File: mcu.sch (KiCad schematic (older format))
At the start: 44 parts

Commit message: Add harmonic filter to ESP32 RF front end.
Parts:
- added C? (x2): CAP-EIA0402, footprints_generic:CAPC100X50X55L30N, symbol gz_Ceramic-Capacitors:CAP-EIA0402
- added L?: IND-EIA0201, footprints_generic:INDC60X30X42L15L, symbol gz_Fixed-Inductors:IND-EIA0201
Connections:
- wire segments 165 -> 172
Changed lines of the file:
@@
 Wire Wire Line
 	3400 4750 3900 4750
+$Comp
+L gz_Ceramic-Capacitors:CAP-EIA0402 C?
+U 1 1 604B4874
+P 6250 5800
+F 0 "C?" V 6200 5950 50  0000 L CNN
+F 1 "CAP-EIA0402" H 6650 6900 50  0001 L CNN
+F 2 "footprints_generic:CAPC100X50X55L30N" H 2950 10150 50  0001 L CNN
+F 3 "${KEMET_MLCC_BASE}C0402C150J5GACTU" H 2950 10250 50  0001 L CNN
+F 4 "Digikey" H 6650 6800 50  0001 L CNN "Vendor"
+F 5 "399-1014-1-ND" H 7000 6800 50  0001 L CNN "Vendor_PN"
+F 6 "KEMET" H 6650 6700 50  0001 L CNN "Manufacturer"
+F 7 "C0402C150J5GACTU" H 7250 6700 50  0001 L CNN "MPN"
+F 8 "Capacitors" H 2950 10550 50  0001 L CNN "Category"
+F 9 "Ceramic Capacitors" H 2950 10650 50  0001 L CNN "Family"
+F 10 "Yes" V 6200 6100 50  0001 L CNN "Fit"
+F 11 "15pF" V 6300 5950 50  0000 L CNN "Capacitance"
+F 12 "±5%" V 6300 6200 50  0000 L CNN "Tolerance"
+F 13 "50V" V 6400 6200 50  0000 L CNN "Voltage"
+F 14 "C0G" V 6400 5950 50  0000 L CNN "Dielectric"
+F 15 "EIA0402" V 6500 5950 50  0000 L CNN "Package"
+	1    6250 5800
+	0    1    1    0
+$EndComp
+$Comp
+L gz_Ceramic-Capacitors:CAP-EIA0402 C?
+U 1 1 604B72FD
+P 7250 5800
+F 0 "C?" V 7200 5950 50  0000 L CNN
+F 1 "CAP-EIA0402" H 7650 6900 50  0001 L CNN
+F 2 "footprints_generic:CAPC100X50X55L30N" H 3950 10150 50  0001 L CNN
+F 3 "${KEMET_MLCC_BASE}C0402C130J5GACTU" H 3950 10250 50  0001 L CNN
+F 4 "Digikey" H 7650 6800 50  0001 L CNN "Vendor"
+F 5 "399-8946-1-ND" H 8000 6800 50  0001 L CNN "Vendor_PN"
+F 6 "KEMET" H 7650 6700 50  0001 L CNN "Manufacturer"
+F 7 "C0402C130J5GACTU" H 8250 6700 50  0001 L CNN "MPN"
+F 8 "Capacitors" H 3950 10550 50  0001 L CNN "Category"
+F 9 "Ceramic Capacitors" H 3950 10650 50  0001 L CNN "Family"
+F 10 "Yes" V 7200 6100 50  0001 L CNN "Fit"
+F 11 "13pF" V 7300 5950 50  0000 L CNN "Capacitance"
+F 12 "±5%" V 7300 6200 50  0000 L CNN "Tolerance"
+F 13 "50V" V 7400 6200 50  0000 L CNN "Voltage"
+F 14 "C0G" V 7400 5950 50  0000 L CNN "Dielectric"
+F 15 "EIA0402" V 7500 5950 50  0000 L CNN "Package"
+	1    7250 5800
+	0    1    1    0
+$EndComp
+$Comp
+L gz_Fixed-Inductors:IND-EIA0201 L?
+U 1 1 604BFB5E
+P 6750 5600
+F 0 "L?" H 6775 5972 50  0000 C CNN
+F 1 "IND-EIA0201" H 7200 7400 50  0001 L CNN
+F 2 "footprints_generic:INDC60X30X42L15L" H 7200 7300 50  0001 L CNN
+F 3 "${MURATA_BASE}LQP03HQ0N6W02%23" H 3450 10050 50  0001 L CNN
+F 4 "Digikey" H 7200 7200 50  0001 L CNN "Vendor"
+F 5 "490-13844-1-ND" H 7550 7200 50  0001 L CNN "Vendor_PN"
+F 6 "Murata Electronics" H 7200 7100 50  0001 L CNN "Manufacturer"
+F 7 "LQP03HQ0N6W02#" H 8000 7100 50  0001 L CNN "MPN"
+F 8 "Inductors, Coils, Chokes" H 7200 7000 50  0001 L CNN "Category"
+F 9 "Fixed Inductors" H 7200 6900 50  0001 L CNN "Family"
+F 10 "Yes" H 6600 6050 50  0001 L CNN "Fit"
+F 11 "0.6Nh" H 6775 5881 50  0000 C CNN "Inductance"
+F 12 "±0.05Nh" H 6775 5790 50  0000 C CNN "Tolerance"
+F 13 "Q 20 @ 500MHz" H 7200 6800 50  0001 L CNN "Quality Factor"
+F 14 "DCR 40mr" H 7200 6700 50  0001 L CNN "DCR"
+F 15 "SRF 20GHz" H 7200 6600 50  0001 L CNN "SRF"
+F 16 "1.1A" H 7200 6500 50  0001 L CNN "Current"
+F 17 "FILM" H 7200 6400 50  0001 L CNN "Type"
+F 18 "EIA0201" H 6775 5699 50  0000 C CNN "Package"
+	1    6750 5600
+	1    0    0    -1
+$EndComp
+Wire Wire Line
+	5950 5600 6250 5600
+Wire Wire Line
+	6250 5700 6250 5600
+Connection ~ 6250 5600
+Wire Wire Line
+	6250 5600 6650 5600
+Wire Wire Line
+	6900 5600 7250 5600
+Wire Wire Line
+	7250 5600 7250 5700
+Wire Wire Line
+	7250 5900 7250 5950
+Wire Wire Line
+	6250 5900 6250 5950
+$Comp
+L gz_Power-Symbols:GND #PWR?
+U 1 1 604F291C
+P 6250 5950
+F 0 "#PWR?" H 6250 5700 50  0001 C CNN
+F 1 "GND" H 6255 5777 50  0000 C CNN
+F 2 "" H 6250 5950 50  0001 C CNN
+F 3 "" H 6250 5950 50  0001 C CNN
+	1    6250 5950
+	1    0    0    -1
+$EndComp
+$Comp
+L gz_Power-Symbols:GND #PWR?
+U 1 1 604F32B0
+P 7250 5950
+F 0 "#PWR?" H 7250 5700 50  0001 C CNN
+F 1 "GND" H 7255 5777 50  0000 C CNN
+F 2 "" H 7250 5950 50  0001 C CNN
+F 3 "" H 7250 5950 50  0001 C CNN
+	1    7250 5950
+	1    0    0    -1
+$EndComp
 $EndSCHEMATC

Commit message: Add antenna matching section.
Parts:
- removed L?: IND-EIA0201, footprints_generic:INDC60X30X42L15L, symbol gz_Fixed-Inductors:IND-EIA0201
- added L?: IND-EIA0402, footprints_generic:INDC100X50X55L25N, symbol gz_Fixed-Inductors:IND-EIA0402
- added Z? (x3): Z-EIA0402, footprints_generic:RESC100X50X40L25NN, symbol gz_Generic-Impedance-Surface-Mount:Z-EIA0402
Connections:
- wire segments 172 -> 180
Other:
- note added: "2445MHz\nQ = 10"
- note added: "30 +j10"
- note added: "50R"
- note added: "Antenna Matching\n"
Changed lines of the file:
@@
 	0    1    1    0
-$EndComp
-$Comp
-L gz_Fixed-Inductors:IND-EIA0201 L?
-U 1 1 604BFB5E
-P 6750 5600
-F 0 "L?" H 6775 5972 50  0000 C CNN
-F 1 "IND-EIA0201" H 7200 7400 50  0001 L CNN
-F 2 "footprints_generic:INDC60X30X42L15L" H 7200 7300 50  0001 L CNN
-F 3 "${MURATA_BASE}LQP03HQ0N6W02%23" H 3450 10050 50  0001 L CNN
-F 4 "Digikey" H 7200 7200 50  0001 L CNN "Vendor"
-F 5 "490-13844-1-ND" H 7550 7200 50  0001 L CNN "Vendor_PN"
-F 6 "Murata Electronics" H 7200 7100 50  0001 L CNN "Manufacturer"
-F 7 "LQP03HQ0N6W02#" H 8000 7100 50  0001 L CNN "MPN"
-F 8 "Inductors, Coils, Chokes" H 7200 7000 50  0001 L CNN "Category"
-F 9 "Fixed Inductors" H 7200 6900 50  0001 L CNN "Family"
-F 10 "Yes" H 6600 6050 50  0001 L CNN "Fit"
-F 11 "0.6Nh" H 6775 5881 50  0000 C CNN "Inductance"
-F 12 "±0.05Nh" H 6775 5790 50  0000 C CNN "Tolerance"
-F 13 "Q 20 @ 500MHz" H 7200 6800 50  0001 L CNN "Quality Factor"
-F 14 "DCR 40mr" H 7200 6700 50  0001 L CNN "DCR"
-F 15 "SRF 20GHz" H 7200 6600 50  0001 L CNN "SRF"
-F 16 "1.1A" H 7200 6500 50  0001 L CNN "Current"
-F 17 "FILM" H 7200 6400 50  0001 L CNN "Type"
-F 18 "EIA0201" H 6775 5699 50  0000 C CNN "Package"
-	1    6750 5600
-	1    0    0    -1
 $EndComp
 Wire Wire Line
@@
 	1    0    0    -1
 $EndComp
+$Comp
+L gz_Fixed-Inductors:IND-EIA0402 L?
+U 1 1 604DAC9B
+P 6750 5600
+F 0 "L?" H 6650 5900 50  0000 L CNN
+F 1 "IND-EIA0402" H 7200 7400 50  0001 L CNN
+F 2 "footprints_generic:INDC100X50X55L25N" H 7200 7300 50  0001 L CNN
+F 3 "${TDK_BASE}MLG1005S0N6BT000" H 3450 10050 50  0001 L CNN
+F 4 "Digikey" H 7200 7200 50  0001 L CNN "Vendor"
+F 5 "445-16237-1-ND" H 7550 7200 50  0001 L CNN "Vendor_PN"
+F 6 "TDK Corporation" H 7200 7100 50  0001 L CNN "Manufacturer"
+F 7 "MLG1005S0N6BT000" H 8000 7100 50  0001 L CNN "MPN"
+F 8 "Inductors, Coils, Chokes" H 7200 7000 50  0001 L CNN "Category"
+F 9 "Fixed Inductors" H 7200 6900 50  0001 L CNN "Family"
+F 10 "Yes" H 6600 6050 50  0001 L CNN "Fit"
+F 11 "0.6nH" H 6650 5800 50  0000 L CNN "Inductance"
+F 12 "±0.1nH" H 6900 5800 50  0000 L CNN "Tolerance"
+F 13 "Q 10 @ 100MHz" H 7200 6800 50  0001 L CNN "Quality Factor"
+F 14 "DCR 100mR" H 7200 6700 50  0001 L CNN "DCR"
+F 15 "SRF 10GHz" H 7200 6600 50  0001 L CNN "SRF"
+F 16 "Imax 1A" H 7200 6500 50  0001 L CNN "Current"
+F 17 "ML" H 7200 6400 50  0001 L CNN "Type"
+F 18 "EIA0402" H 6650 5700 50  0000 L CNN "Package"
+	1    6750 5600
+	1    0    0    -1
+$EndComp
+Text Notes 5700 5950 0    50   ~ 0
+30 +j10
+Wire Notes Line
+	7850 5150 7850 6250
+Wire Notes Line
+	7850 6250 6050 6250
+Wire Notes Line
+	6050 6250 6050 5150
+Wire Notes Line
+	6050 5150 7850 5150
+Wire Notes Line style solid
+	6000 5850 6000 5650
+Wire Notes Line style solid
+	6000 5650 5900 5650
+Wire Notes Line style solid
+	5900 5650 5925 5625
+Wire Notes Line style solid
+	5900 5650 5925 5675
+Text Notes 7900 5950 0    50   ~ 0
+50R
+Wire Notes Line style solid
+	8000 5850 8000 5650
+Wire Notes Line style solid
+	8000 5650 7900 5650
+Wire Notes Line style solid
+	7900 5650 7925 5625
+Wire Notes Line style solid
+	7900 5650 7925 5675
+Connection ~ 7250 5600
+Text Notes 7450 5350 0    50   ~ 0
+2445MHz\nQ = 10
+Wire Wire Line
+	8650 5650 8650 5600
+Connection ~ 8650 5600
+Wire Wire Line
+	9250 5600 9500 5600
+Wire Wire Line
+	9500 5600 9500 5650
+Wire Wire Line
+	8650 5950 8650 6000
+$Comp
+L gz_Power-Symbols:GND #PWR?
+U 1 1 605A2506
+P 8650 6000
+F 0 "#PWR?" H 8650 5750 50  0001 C CNN
+F 1 "GND" H 8655 5827 50  0000 C CNN
+F 2 "" H 8650 6000 50  0001 C CNN
+F 3 "" H 8650 6000 50  0001 C CNN
+	1    8650 6000
+	1    0    0    -1
+$EndComp
+Wire Notes Line
+	10250 5150 10250 6250
+Wire Notes Line
+	10250 6250 8450 6250
+Wire Notes Line
+	8450 6250 8450 5150
+Wire Notes Line
+	8450 5150 10250 5150
+Text Notes 10300 5950 0    50   ~ 0
+50R
+Wire Notes Line style solid
+	10400 5850 10400 5650
+Wire Notes Line style solid
+	10400 5650 10300 5650
+Wire Notes Line style solid
+	10300 5650 10325 5625
+Wire Notes Line style solid
+	10300 5650 10325 5675
+Wire Wire Line
+	9500 5600 10400 5600
+Connection ~ 9500 5600
+Wire Wire Line
+	7250 5600 8650 5600
+Text Notes 8400 5950 2    50   ~ 0
+50R
+Wire Notes Line style solid
+	8300 5850 8300 5650
+Wire Notes Line style solid
+	8300 5650 8400 5650
+Wire Notes Line style solid
+	8400 5650 8375 5625
+Wire Notes Line style solid
+	8400 5650 8375 5675
+$Comp
+L gz_Generic-Impedance-Surface-Mount:Z-EIA0402 Z?
+U 1 1 605FEF00
+P 8650 5800
+F 0 "Z?" V 8559 5853 50  0000 L CNN
+F 1 "Z-EIA0402" H 9450 6700 50  0001 L CNN
+F 2 "footprints_generic:RESC100X50X40L25NN" H 5350 10150 50  0001 L CNN
+F 3 "" H 5350 10250 50  0001 L CNN
+F 4 "TBD" H 9450 6600 50  0001 L CNN "Vendor"
+F 5 "TBD" H 9800 6600 50  0001 L CNN "Vendor_PN"
+F 6 "TBD" H 9450 6500 50  0001 L CNN "Manufacturer"
+F 7 "TBD" H 10050 6500 50  0001 L CNN "MPN"
+F 8 "TBD" H 5350 10550 50  0001 L CNN "Category"
+F 9 "TBD" H 5350 10650 50  0001 L CNN "Family"
+F 10 "NF" V 8650 5853 50  0000 L CNN "Fit"
+F 11 "TBD" V 8695 5853 50  0001 L CNN "Nominal"
+F 12 "TBD" V 8695 5853 50  0001 L CNN "Tolerance"
+F 13 "EIA0402" V 8741 5853 50  0000 L CNN "Package"
+	1    8650 5800
+	0    1    1    0
+$EndComp
+Wire Wire Line
+	9500 5950 9500 6000
+$Comp
+L gz_Power-Symbols:GND #PWR?
+U 1 1 6063A4C0
+P 9500 6000
+F 0 "#PWR?" H 9500 5750 50  0001 C CNN
+F 1 "GND" H 9505 5827 50  0000 C CNN
+F 2 "" H 9500 6000 50  0001 C CNN
+F 3 "" H 9500 6000 50  0001 C CNN
+	1    9500 6000
+	1    0    0    -1
+$EndComp
+$Comp
+L gz_Generic-Impedance-Surface-Mount:Z-EIA0402 Z?
+U 1 1 6063A4D0
+P 9500 5800
+F 0 "Z?" V 9409 5853 50  0000 L CNN
+F 1 "Z-EIA0402" H 10300 6700 50  0001 L CNN
+F 2 "footprints_generic:RESC100X50X40L25NN" H 6200 10150 50  0001 L CNN
+F 3 "" H 6200 10250 50  0001 L CNN
+F 4 "TBD" H 10300 6600 50  0001 L CNN "Vendor"
+F 5 "TBD" H 10650 6600 50  0001 L CNN "Vendor_PN"
+F 6 "TBD" H 10300 6500 50  0001 L CNN "Manufacturer"
+F 7 "TBD" H 10900 6500 50  0001 L CNN "MPN"
+F 8 "TBD" H 6200 10550 50  0001 L CNN "Category"
+F 9 "TBD" H 6200 10650 50  0001 L CNN "Family"
+F 10 "NF" V 9500 5853 50  0000 L CNN "Fit"
+F 11 "TBD" V 9545 5853 50  0001 L CNN "Nominal"
+F 12 "TBD" V 9545 5853 50  0001 L CNN "Tolerance"
+F 13 "EIA0402" V 9591 5853 50  0000 L CNN "Package"
+	1    9500 5800
+	0    1    1    0
+$EndComp
+$Comp
+L gz_Generic-Impedance-Surface-Mount:Z-EIA0402 Z?
+U 1 1 6067079F
+P 9100 5600
+F 0 "Z?" H 9150 5500 50  0000 L CNN
+F 1 "Z-EIA0402" H 9900 6500 50  0001 L CNN
+F 2 "footprints_generic:RESC100X50X40L25NN" H 5800 9950 50  0001 L CNN
+F 3 "" H 5800 10050 50  0001 L CNN
+F 4 "TBD" H 9900 6400 50  0001 L CNN "Vendor"
+F 5 "TBD" H 10250 6400 50  0001 L CNN "Vendor_PN"
+F 6 "TBD" H 9900 6300 50  0001 L CNN "Manufacturer"
+F 7 "TBD" H 10500 6300 50  0001 L CNN "MPN"
+F 8 "TBD" H 5800 10350 50  0001 L CNN "Category"
+F 9 "TBD" H 5800 10450 50  0001 L CNN "Family"
+F 10 "Yes" H 9200 5400 50  0001 L CNN "Fit"
+F 11 "0R" H 8950 5500 50  0000 L CNN "Nominal"
+F 12 "TBD" V 9145 5653 50  0001 L CNN "Tolerance"
+F 13 "EIA0402" H 8950 5700 50  0000 L CNN "Package"
+	1    9100 5600
+	-1   0    0    1
+$EndComp
+Wire Wire Line
+	8650 5600 8950 5600
+Text Notes 8500 5250 0    50   ~ 0
+Antenna Matching\n
 $EndSCHEMATC

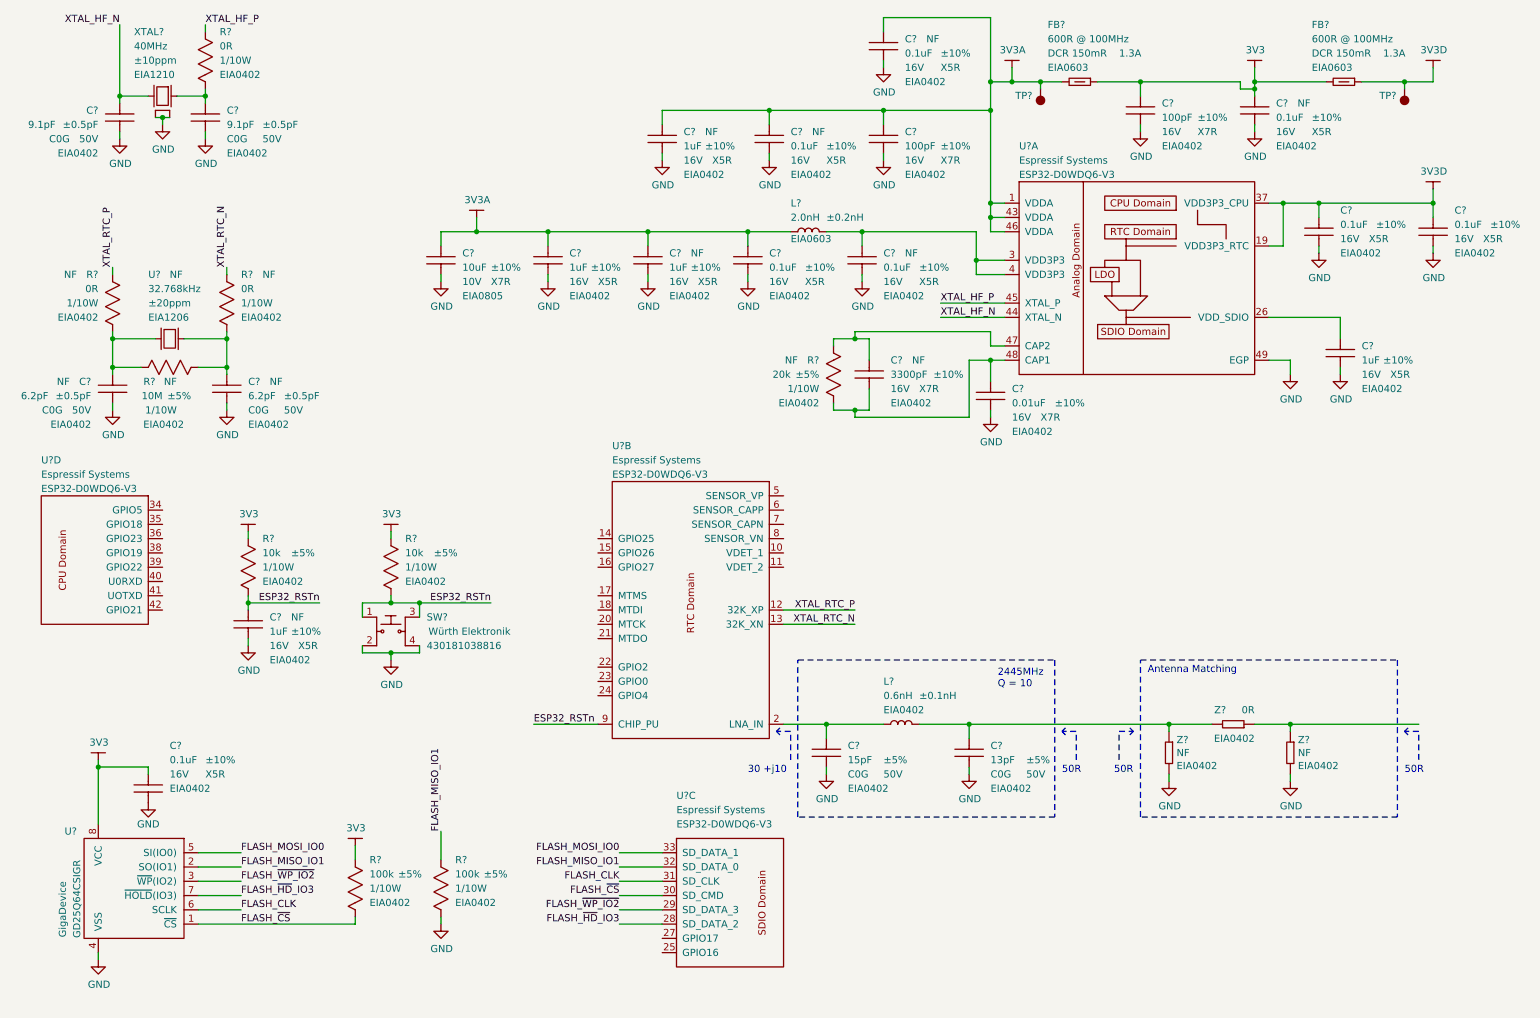
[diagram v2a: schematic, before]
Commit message: Separate MCU I/O sections in their own sheet.
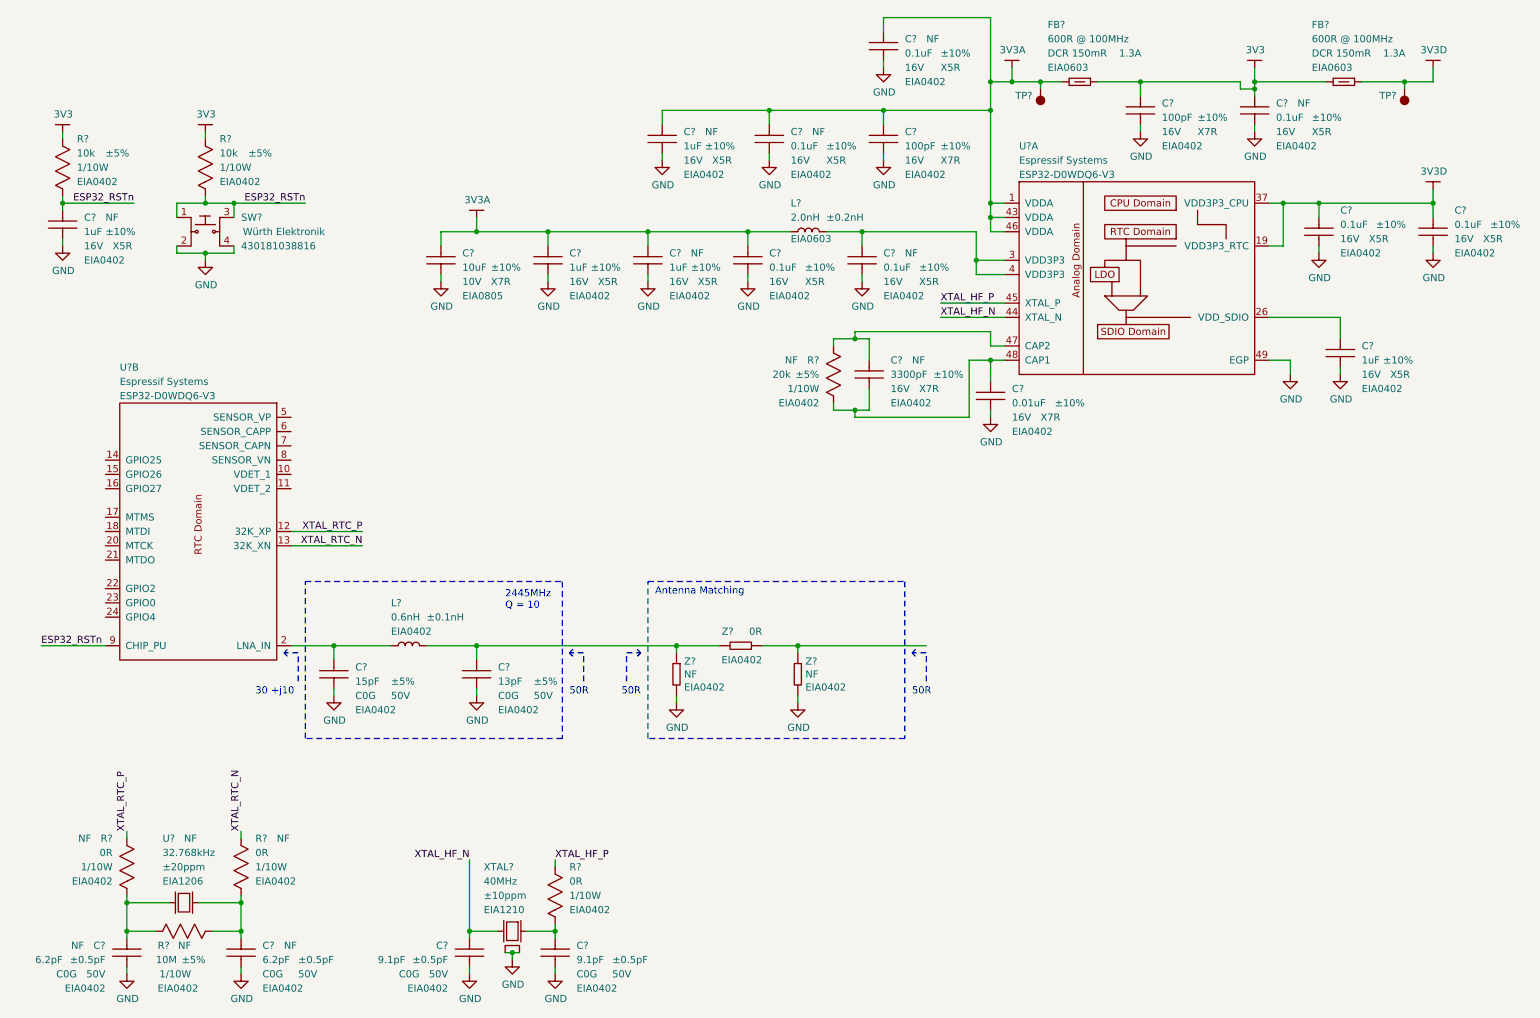
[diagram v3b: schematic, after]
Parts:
- removed C? (x2): CAP-EIA0402, footprints_generic:CAPC100X50X55L30N, symbol gz_Ceramic-Capacitors:CAP-EIA0402
- removed R? (x4): RES-EIA0402, footprints_generic:RESC100X50X40L25NN, symbol gz_Chip-Resistors-Surface-Mount:RES-EIA0402
- removed SW?: WE-430181038816, footprints:WE-430181038816_SWSOFL4P150_450X750X380L150X70N, symbol gz_Tactile-Switches:WE-430181038816
- removed U?: GigaDevice-GD25Q64CSIGR, footprints:Espressif-ESP32_QFN49P40_600X600X90L40X20T430N, symbol gz_Memory:GigaDevice-GD25Q64CSIGR
- removed U? (x2): Espressif_ESP32-D0WDQ6-V3, footprints:Espressif-ESP32_QFN49P40_600X600X90L40X20T430N, symbol gz_RF-Transceiver-ICs:Espressif_ESP32-D0WDQ6-V3
- added C?: CAP-EIA0402, footprints_generic:CAPC100X50X55L30N, symbol gz_Ceramic-Capacitors:CAP-EIA0402
- added R? (x2): RES-EIA0402, footprints_generic:RESC100X50X40L25NN, symbol gz_Chip-Resistors-Surface-Mount:RES-EIA0402
- added SW?: WE-430181038816, footprints:WE-430181038816_SWSOFL4P150_450X750X380L150X70N, symbol gz_Tactile-Switches:WE-430181038816
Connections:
- net +3V3: now also R?.1, R?.1
- net ESP32_RSTn: now also C?.1, R?.2, R?.2, SW?.1, SW?.3
- net GND: now also C?.2, SW?.2, SW?.4
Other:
- moved on the sheet: C?, L?, R?, U?, U?B, XTAL?, Z?
